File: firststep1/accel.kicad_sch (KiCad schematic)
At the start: 12 parts, among them J1 Conn_01x02, J2 Conn_01x03_Male, U1 LM317_TO-220, U2 TL431LP

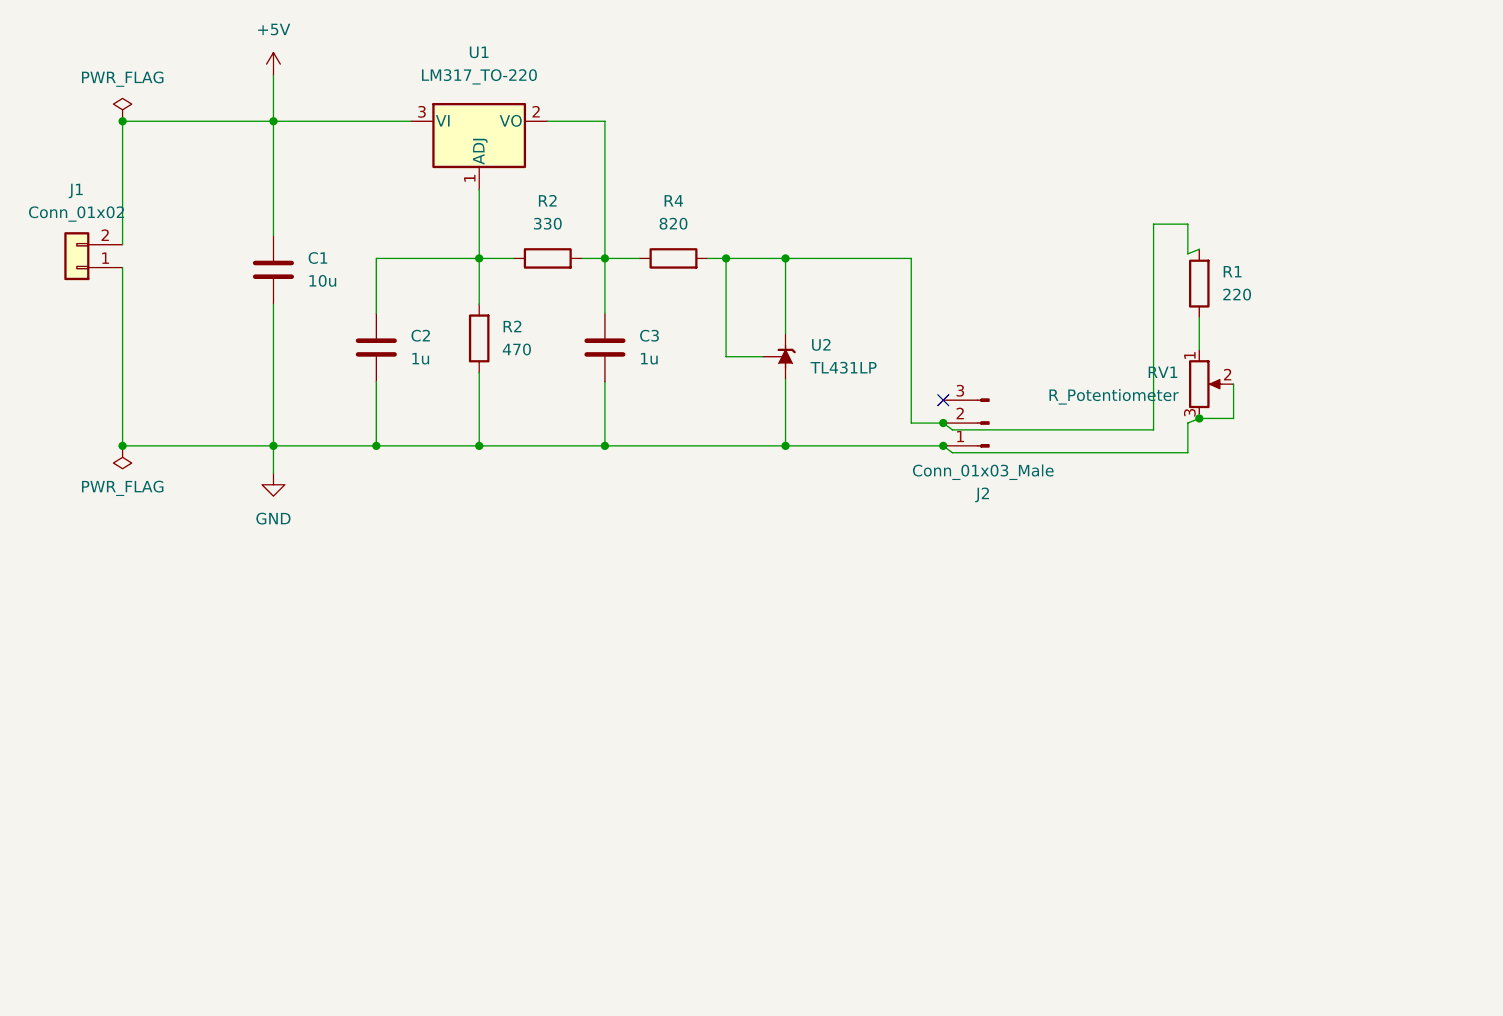
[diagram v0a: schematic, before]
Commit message: added kicad opeamp
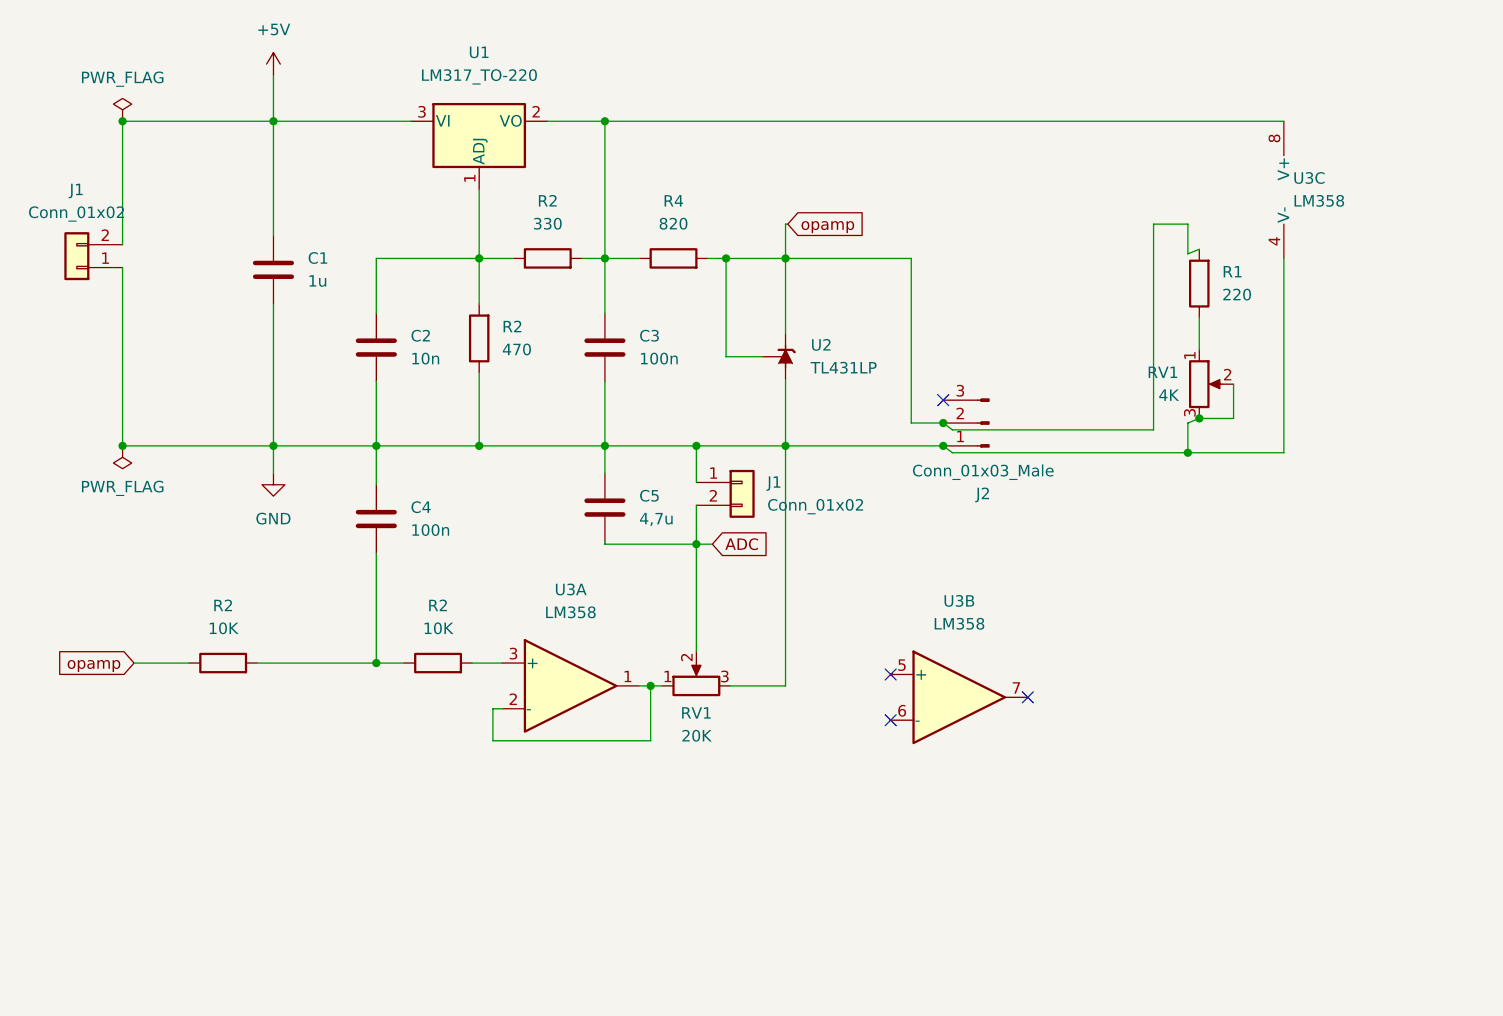
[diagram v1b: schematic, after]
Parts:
- added C4: 100n, Capacitor_THT:C_Disc_D3.0mm_W2.0mm_P2.50mm, symbol Device:C
- added C5: 4,7u, Capacitor_THT:C_Disc_D8.0mm_W2.5mm_P5.00mm, symbol Device:C
- added J1: Conn_01x02, Connector_Wago:Wago_734-162_1x02_P3.50mm_Horizontal, symbol Connector_Generic:Conn_01x02
- added R2 (x2): 330, R_Axial_DIN0207_L6.3mm_D2.5mm_P7.62mm_Horizontal, symbol Device:R
- added RV1: R_Potentiometer, Potentiometer_THT:Potentiometer_ACP_CA9-V10_Vertical, symbol Device:R_Potentiometer
- added U3: LM358, symbol Amplifier_Operational:LM358
- C2: value 1u -> 10n
- C3: value 1u -> 100n
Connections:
- net GND: now also C4.1, C5.1, J1.1 (Pin_1), RV1.3, U3.4 (V-)
- net opamp: now reaches J2.2 (Pin_2), R1.2, R4.2, U2.1 (REF), U2.3 (K)
- net opamp: now also R2.1
- net at C3.1, R2.2, R4.1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: now also U3.8 (V+)
- new net: RV1.1, U3.1, U3.2 (-)
- new net: C4.2, R2.1, R2.2
- new net: R2.2, U3.3 (+)
- new net ADC: C5.2, J1.2 (Pin_2), RV1.2
- no-connect marks 1 -> 4

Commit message: added suppression diode, changed cap values
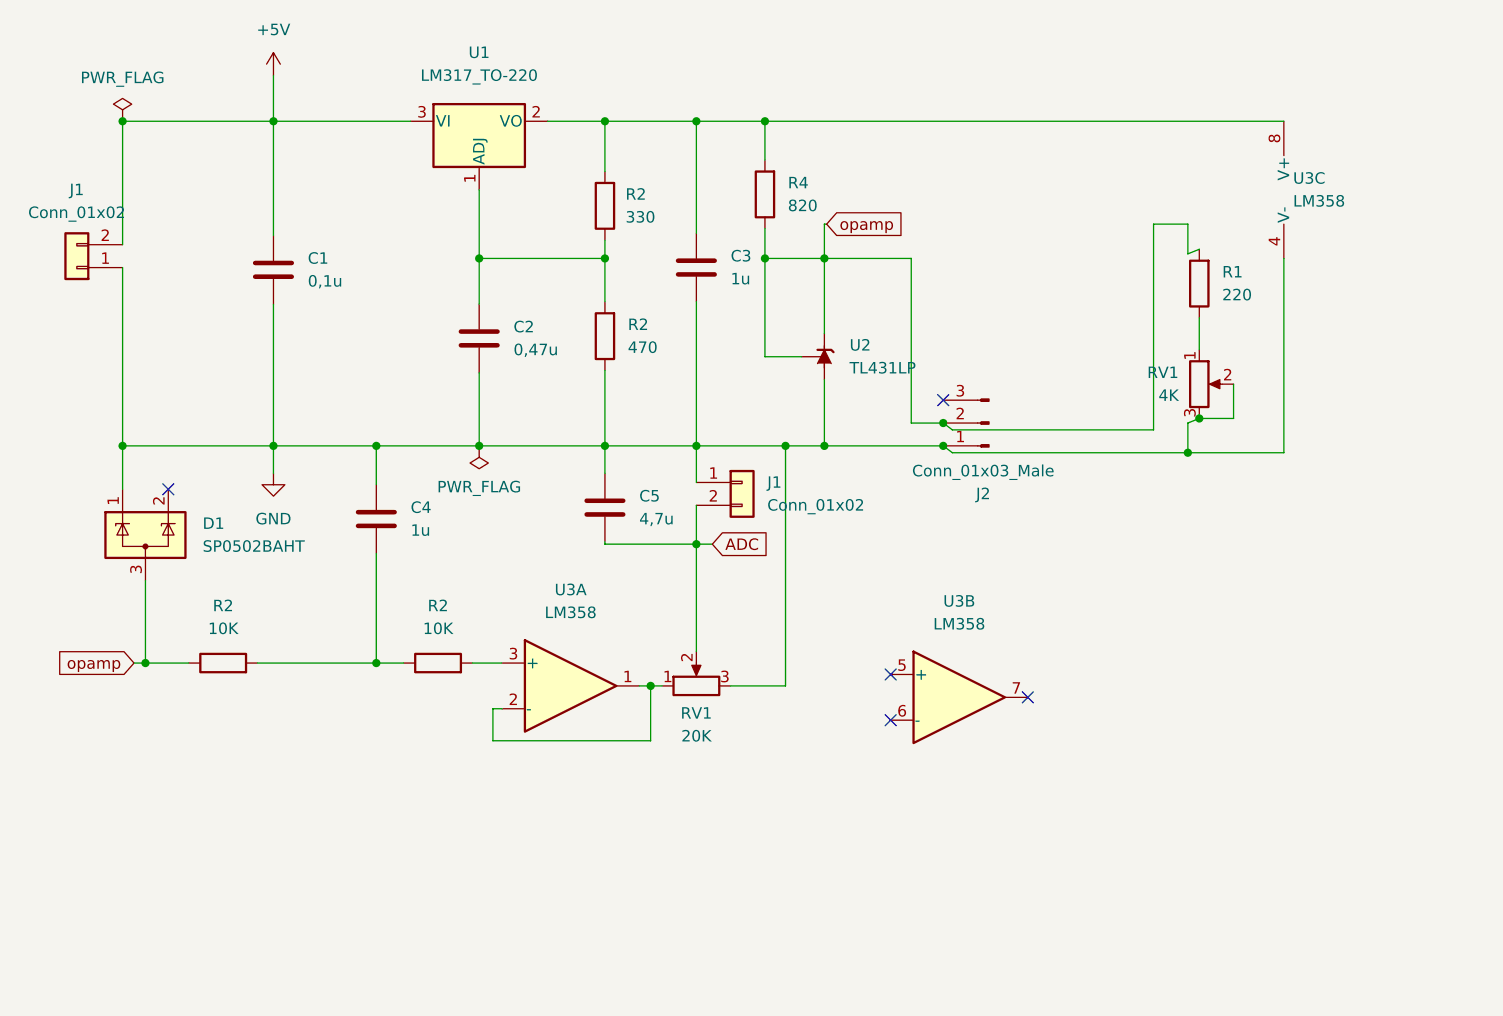
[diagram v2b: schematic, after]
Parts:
- added D1: SP0502BAHT, Package_TO_SOT_SMD:SOT-23, symbol Power_Protection:SP0502BAHT
- C2: value 10n -> 0,47u
- C3, C4: value 100n -> 1u
- U3: footprint (none) -> Package_DIP:DIP-8_W7.62mm
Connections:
- net GND: now also D1.1 (K)
- net opamp: now also R4.1, D1.3 (A); no longer R4.2
- net at C3.1, R2.2, U1.2 (VO)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: now also R4.2; no longer R4.1
- no-connect marks 4 -> 5
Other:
- moved on the sheet: C2, C3, R2, R4, U2

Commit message: many changes
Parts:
- removed J1: Conn_01x02, Connector_Wago:Wago_734-162_1x02_P3.50mm_Horizontal, symbol Connector_Generic:Conn_01x02
- C5: value 4,7u -> 0,05; footprint Capacitor_THT:C_Disc_D8.0mm_W2.5mm_P5.00mm -> Capacitor_THT:C_Disc_D3.0mm_W1.6mm_P2.50mm
- R1: value 220 -> 150
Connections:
- net +5V renamed 5VDC
- net ADC renamed ADC6
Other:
- moved on the sheet: C1, C2, C3, C4, C5, D1, J1, J2, R1, R2, R4, RV1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

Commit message: minor
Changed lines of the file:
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@@
     (pin "2")
-  )
-  (symbol (lib_id "power:PWR_FLAG") (at 82.804 95.504 180) (unit 1)
-    (in_bom yes) (on_board yes) (fields_autoplaced)
-    (property "Reference" "#FLG02" (id 0) (at 82.804 97.409 0)
-      (effects (font (size 1.27 1.27)) hide)
-    )
-    (property "Value" "PWR_FLAG" (id 1) (at 82.804 100.076 0))
-    (property "Footprint" "" (id 2) (at 82.804 95.504 0)
-      (effects (font (size 1.27 1.27)) hide)
-    )
-    (property "Datasheet" "~" (id 3) (at 82.804 95.504 0)
-      (effects (font (size 1.27 1.27)) hide)
-    )
-    (pin "1")
   )
   (symbol (lib_id "Device:C") (at 106.934 75.692 0) (unit 1)
